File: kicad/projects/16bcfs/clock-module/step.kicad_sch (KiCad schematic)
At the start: 6 parts, among them SW5 SW_SPDT, U9 NE555D

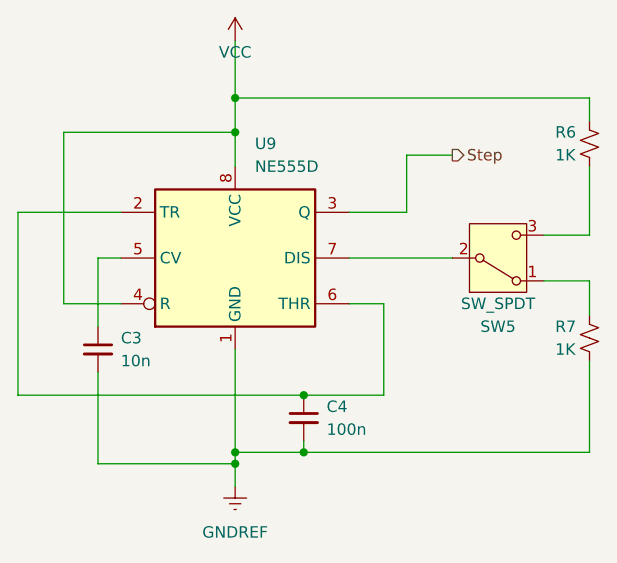
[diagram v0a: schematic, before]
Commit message: Clean up the Reset and Clock Modules
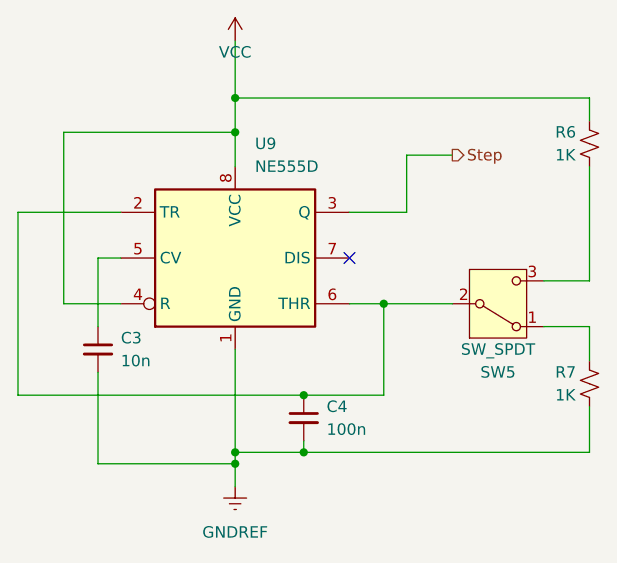
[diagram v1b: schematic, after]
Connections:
- net at SW5.2 (B): now also C4.1, U9.2 (TR), U9.6 (THR); no longer U9.7 (DIS)
- no-connect marks 0 -> 1
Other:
- moved on the sheet: R7, SW5
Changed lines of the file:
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@@
   (junction (at 118.11 100.33) (diameter 0) (color 0 0 0 0)
   )
+  (junction (at 134.62 82.55) (diameter 0) (color 0 0 0 0)
+  )
+  (no_connect (at 130.81 77.47))
   (wire (pts (xy 105.41 77.47) (xy 102.87 77.47))
     (stroke (width 0) (type default))
@@
     (stroke (width 0) (type default))
   )
-  (wire (pts (xy 152.4 74.93) (xy 157.48 74.93))
+  (wire (pts (xy 152.4 80.01) (xy 157.48 80.01))
     (stroke (width 0) (type default))
   )
@@
     (stroke (width 0) (type default))
   )
-  (wire (pts (xy 157.48 80.01) (xy 157.48 83.82))
-    (stroke (width 0) (type default))
-  )
-  (wire (pts (xy 157.48 88.9) (xy 157.48 99.06))
+  (wire (pts (xy 157.48 85.09) (xy 157.48 88.9))
+    (stroke (width 0) (type default))
+  )
+  (wire (pts (xy 134.62 82.55) (xy 142.24 82.55))
+    (stroke (width 0) (type default))
+  )
+  (wire (pts (xy 157.48 93.98) (xy 157.48 99.06))
     (stroke (width 0) (type default))
   )
@@
     (stroke (width 0) (type default))
   )
-  (wire (pts (xy 157.48 74.93) (xy 157.48 67.31))
+  (wire (pts (xy 157.48 80.01) (xy 157.48 67.31))
     (stroke (width 0) (type default))
   )
@@
     (stroke (width 0) (type default))
   )
-  (wire (pts (xy 130.81 77.47) (xy 142.24 77.47))
-    (stroke (width 0) (type default))
-  )
   (wire (pts (xy 105.41 72.39) (xy 93.98 72.39))
     (stroke (width 0) (type default))
@@
     (stroke (width 0) (type default))
   )
-  (wire (pts (xy 152.4 80.01) (xy 157.48 80.01))
+  (wire (pts (xy 152.4 85.09) (xy 157.48 85.09))
     (stroke (width 0) (type default))
   )
@@
     )
   )
-  (symbol (lib_id "Device:R_Small_US") (at 157.48 86.36 0) (unit 1)
-    (in_bom yes) (on_board yes) (dnp no)
-    (property "Reference" "R7" (at 153.67 85.09 0)
-      (effects (font (size 1.27 1.27)) (justify left))
-    )
-    (property "Value" "1K" (at 153.67 87.63 0)
-      (effects (font (size 1.27 1.27)) (justify left))
-    )
-    (property "Footprint" "" (at 157.48 86.36 0)
-      (effects (font (size 1.27 1.27)) hide)
-    )
-    (property "Datasheet" "~" (at 157.48 86.36 0)
+  (symbol (lib_id "Device:R_Small_US") (at 157.48 91.44 0) (unit 1)
+    (in_bom yes) (on_board yes) (dnp no)
+    (property "Reference" "R7" (at 153.67 90.17 0)
+      (effects (font (size 1.27 1.27)) (justify left))
+    )
+    (property "Value" "1K" (at 153.67 92.71 0)
+      (effects (font (size 1.27 1.27)) (justify left))
+    )
+    (property "Footprint" "" (at 157.48 91.44 0)
+      (effects (font (size 1.27 1.27)) hide)
+    )
+    (property "Datasheet" "~" (at 157.48 91.44 0)
       (effects (font (size 1.27 1.27)) hide)
     )
@@
     )
   )
-  (symbol (lib_id "Switch:SW_SPDT") (at 147.32 77.47 0) (mirror x) (unit 1)
-    (in_bom yes) (on_board yes) (dnp no)
-    (property "Reference" "SW5" (at 147.32 85.09 0)
+  (symbol (lib_id "Switch:SW_SPDT") (at 147.32 82.55 0) (mirror x) (unit 1)
+    (in_bom yes) (on_board yes) (dnp no)
+    (property "Reference" "SW5" (at 147.32 90.17 0)
       (effects (font (size 1.27 1.27)))
     )
-    (property "Value" "SW_SPDT" (at 147.32 82.55 0)
+    (property "Value" "SW_SPDT" (at 147.32 87.63 0)
       (effects (font (size 1.27 1.27)))
     )
-    (property "Footprint" "" (at 147.32 77.47 0)
-      (effects (font (size 1.27 1.27)) hide)
-    )
-    (property "Datasheet" "~" (at 147.32 77.47 0)
-      (effects (font (size 1.27 1.27)) hide)
-    )
+    (property "Footprint" "" (at 147.32 82.55 0)
+      (effects (font (size 1.27 1.27)) hide)
+    )
+    (property "Datasheet" "~" (at 147.32 82.55 0)
+      (effects (font (size 1.27 1.27)) hide)
+    )
